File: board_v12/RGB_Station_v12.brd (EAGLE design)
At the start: 86.4 x 17.8 mm, 44 parts, among them IC1 MCP1702T-3302E/MB, J1 M20, J2 M20, J3 USB_MICRO, SW1 KMR2_SWITCH, SW2 KMR2_SWITCH, U1 PIC32MX270F256D_44VTLA_44, U2 74LVC2T45, U3 MCP121T-315E/TT, U4 DSC6111CI1A-008.0000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

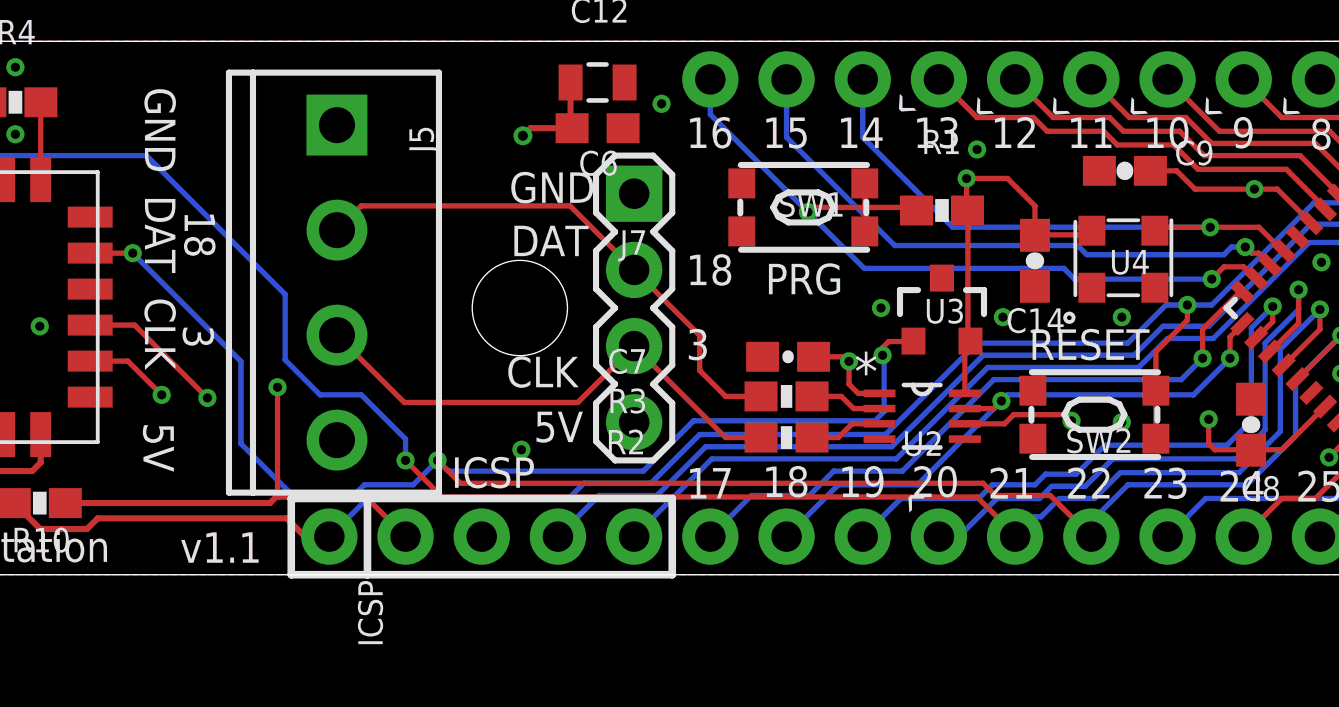
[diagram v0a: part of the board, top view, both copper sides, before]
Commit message: Created v1.2 : fixed schematic problem with switches being always grounded.
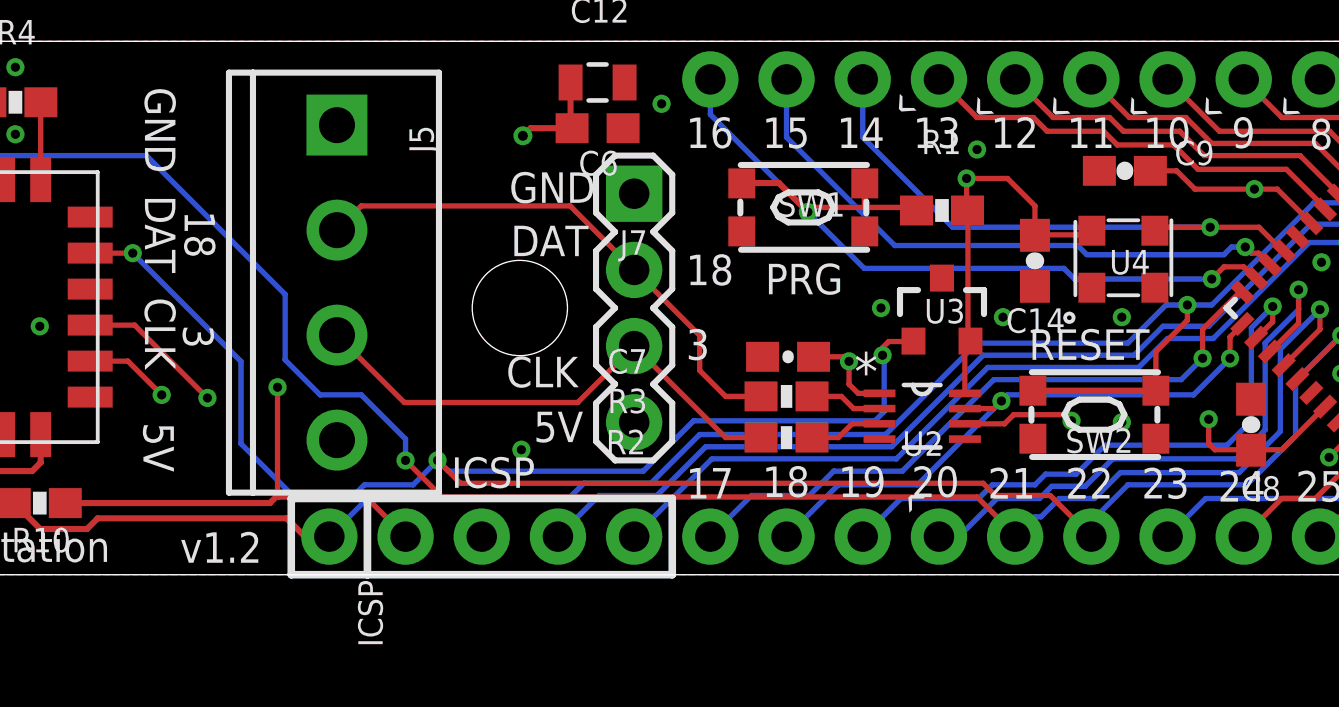
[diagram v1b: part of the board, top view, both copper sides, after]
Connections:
- net !MCLR!: now also SW2.P1; no longer SW2.P3
- net GND: now also SW1.P3, SW2.P3; no longer SW1.P1, SW2.P1
- net RA8: now also SW1.P1; no longer SW1.P3
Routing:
- net !MCLR!: track 90.3 -> 92.8 mm
- net RA8: track 27.4 -> 29.1 mm
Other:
- board text added: "v1.2"
- board text removed: "v1.1"

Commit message: Updates to v1.2 : Made two screw terminals DNPs, and changed C2 from .1uf to 1uF to help with preventing resetting of PIC32 when RN does firmware update.
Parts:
- C2: value .1uF -> 1uF
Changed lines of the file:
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@@
 <?xml version="1.0" encoding="utf-8"?>
 <!DOCTYPE eagle SYSTEM "eagle.dtd">
-<eagle version="7.7.0">
+<eagle version="8.6.2">
 <drawing>
 <settings>
-<setting alwaysvectorfont="yes"/>
+<setting alwaysvectorfont="no"/>
+<setting keepoldvectorfont="yes"/>
 <setting verticaltext="up"/>
 </settings>
@@
 <param name="dpMaxLengthDifference" value="10mm"/>
 <param name="dpGapFactor" value="2.5"/>
-<param name="checkGrid" value="0"/>
 <param name="checkAngle" value="1"/>
 <param name="checkFont" value="1"/>
 <param name="checkRestrict" value="0"/>
+<param name="checkStop" value="0"/>
+<param name="checkValues" value="0"/>
 <param name="useDiameter" value="13"/>
 <param name="maxErrors" value="50"/>
@@
 <element name="U$4" library="SchmalzHausPublic" package="CHIPKIT_2MM" value="CHIPKIT2MM" x="84.99" y="0.6452" rot="MR0"/>
 <element name="J5" library="SparkFun-Connectors" package="SCREWTERMINAL-3.5MM-4@1" value="" x="15.494" y="14.986" smashed="yes" rot="R270">
+<attribute name="NAME" x="17.907" y="14.986" size="0.8128" layer="25" font="vector" ratio="10" rot="R270"/>
+<attribute name="PROD_ID" value="2xCONN-08399" x="-22.606" y="61.976" size="1.778" layer="27" rot="R270" display="off"/>
 <attribute name="SF_ID" value="2xPRT-08084" x="-22.606" y="61.976" size="1.778" layer="27" rot="R270" display="off"/>
-<attribute name="PROD_ID" value="2xCONN-08399" x="-22.606" y="61.976" size="1.778" layer="27" rot="R270" display="off"/>
-<attribute name="NAME" x="17.907" y="14.986" size="0.8128" layer="25" font="vector" ratio="10" rot="R270"/>
 <attribute name="VALUE" x="13.208" y="14.986" size="0.6096" layer="27" font="vector" ratio="20" rot="R270"/>
 </element>
@@
 </element>
 <element name="J7" library="SparkFun-Connectors" package="1X04" value="" x="25.4" y="12.7" smashed="yes" rot="R270">
+<attribute name="NAME" x="24.9174" y="10.668" size="0.8128" layer="25" font="vector" ratio="10"/>
 <attribute name="PROD_ID" value="CONN-09696" x="72.39" y="95.25" size="1.778" layer="27" rot="R270" display="off"/>
-<attribute name="NAME" x="24.9174" y="10.668" size="0.8128" layer="25" font="vector" ratio="10"/>
 <attribute name="VALUE" x="22.225" y="13.97" size="1.27" layer="27" rot="R270"/>
 </element>
@@
 </element>
 <element name="J3" library="SparkFun-Connectors" package="USB-B-MICRO-SMD" value="USB_MICRO" x="84.328" y="5.4356" smashed="yes" rot="R180">
+<attribute name="NAME" x="85.598" y="0.7366" size="0.8128" layer="25" font="vector" ratio="10" rot="R180"/>
 <attribute name="PROD_ID" value="CONN-11752" x="84.328" y="5.4356" size="1.778" layer="27" rot="R180" display="off"/>
-<attribute name="NAME" x="85.598" y="0.7366" size="0.8128" layer="25" font="vector" ratio="10" rot="R180"/>
 <attribute name="VALUE" x="85.598" y="10.1346" size="0.8128" layer="27" font="vector" ratio="10" rot="R180" align="top-left"/>
 </element>
 <element name="J6" library="SparkFun-Connectors" package="SCREWTERMINAL-3.5MM-2" value="" x="81.3308" y="15.6972" smashed="yes" rot="R270">
 <attribute name="NAME" x="84.7598" y="16.9672" size="0.8128" layer="25" font="vector" ratio="10" rot="R270"/>
+<attribute name="PROD_ID" value="CONN-08399" x="81.3308" y="15.6972" size="1.778" layer="27" rot="R270" display="off"/>
 <attribute name="VALUE" x="77.2668" y="16.9672" size="0.6096" layer="27" font="vector" ratio="20" rot="R270"/>
-<attribute name="PROD_ID" value="CONN-08399" x="81.3308" y="15.6972" size="1.778" layer="27" rot="R270" display="off"/>
 </element>
 <element name="U3" library="MCP1x2_ResetController" package="SOT23-3" value="MCP121T-315E/TT" x="35.6616" y="8.7884" smashed="yes">
@@
 <attribute name="VALUE" x="0.4064" y="16.5481" size="0.8128" layer="27" font="vector" ratio="10"/>
 </element>
-<element name="C2" library="SparkFun-Capacitors" package="0603-CAP" value=".1uF" x="2.3876" y="2.3876" smashed="yes">
+<element name="C2" library="SparkFun-Capacitors" package="0603-CAP" value="1uF" x="2.3876" y="2.3876" smashed="yes">
 <attribute name="NAME" x="1.7018" y="0.762" size="0.8128" layer="25" font="vector" ratio="10"/>
 <attribute name="VALUE" x="1.2192" y="-0.5334" size="0.8128" layer="27" font="vector" ratio="10"/>

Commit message: Updated v1.2 board for PCB:NG production - changed DRC rules to minimize violations. Updated .1uF cap and red LED with alternate parts. Updated USB footprint to be exactly correct for Wurth USB connector from BOM
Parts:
- IC1: device linear:SOT89 -> RGB_Station_v12:LINEAR_SOT89
- J3: device SparkFun-Connectors:USB-B-MICRO-SMD -> RGB_Station_v12:SPARKFUN-CONNECTORS_USB-B-MICRO-SMD
- moved J3 0.46 mm to (84.8, 5.44)
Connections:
- removed net N$8: C2.1, U6.5
- new net N$7: C2.1, U6.9
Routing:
- net N$7: track 0.00 -> 15.8 mm, vias 0 -> 2
- net N$8: track 5.58 -> 0.00 mm
- net RC7: track 6.06 -> 5.31 mm
- net USBID/RB5: track 53.7 -> 54.2 mm
- net D-/RB11: track 33.6 -> 34.1 mm
- net D+/RB10: track 36.7 -> 37.2 mm
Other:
- board size 86.4 x 17.8 mm -> 86.4 x 18.2 mm

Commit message: Updated note on schematic about using open-drain reset controller, not push-pull.
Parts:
- U3: value MCP121T-315E/TT -> MCP131T-315E/TT
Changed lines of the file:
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@@
 <attribute name="VALUE" x="77.2668" y="16.9672" size="0.6096" layer="27" font="vector" ratio="20" rot="R270"/>
 </element>
-<element name="U3" library="MCP1x2_ResetController" package="SOT23-3" value="MCP121T-315E/TT" x="35.6616" y="8.7884" smashed="yes">
+<element name="U3" library="MCP1x2_ResetController" package="SOT23-3" value="MCP131T-315E/TT" x="35.6616" y="8.7884" smashed="yes">
 <attribute name="NAME" x="35.068" y="8.3792" size="0.8128" layer="25" font="vector" ratio="10"/>
 <attribute name="VALUE" x="23.5364" y="8.8604" size="0.8128" layer="27" font="vector" ratio="10"/>

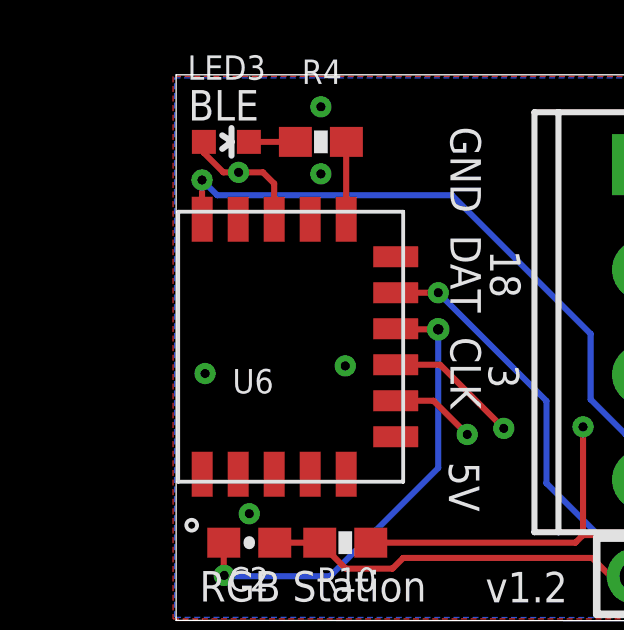
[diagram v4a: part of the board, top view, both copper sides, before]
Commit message: Finished centroid file for PCB:NG automation. Updated some library footprints.
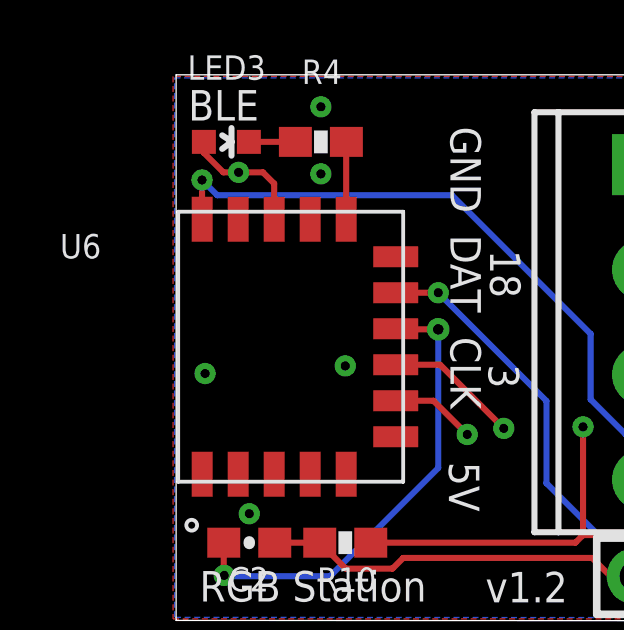
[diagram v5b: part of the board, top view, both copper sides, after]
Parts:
- IC1: device RGB_Station_v12:LINEAR_SOT89 -> RGB_Station_v12_VREG:RGB_STATION_V12_LINEAR_SOT89
- J3: device RGB_Station_v12:SPARKFUN-CONNECTORS_USB-B-MICRO-SMD -> RGB_Station_v12_USB_CONN:SPARKFUN-CONNECTORS_USB-B-MICRO-SMD
- moved U6 7.30 mm to (1.77, 8.92)

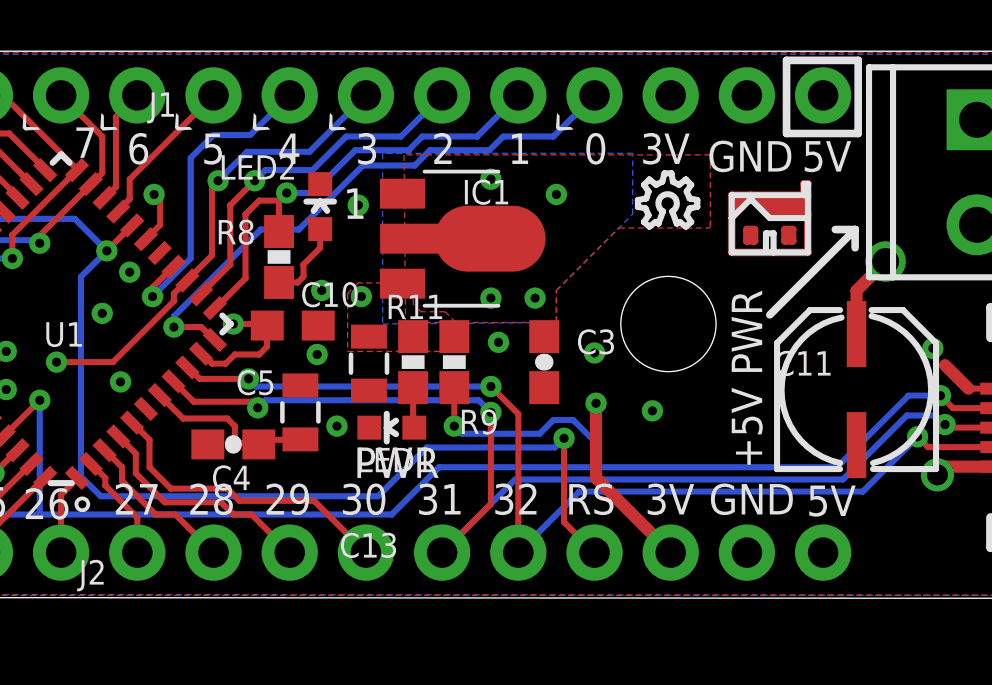
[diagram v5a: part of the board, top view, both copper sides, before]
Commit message: Got all PCB:NG DFM errors to go away - * Added large stop mask rectangles custom versions of USB, level shifter and PIC32 parts to fix stop mask too close errors * Fixed CAM file to include pads layer when generating inner layer gerbers to fix annular ring errors
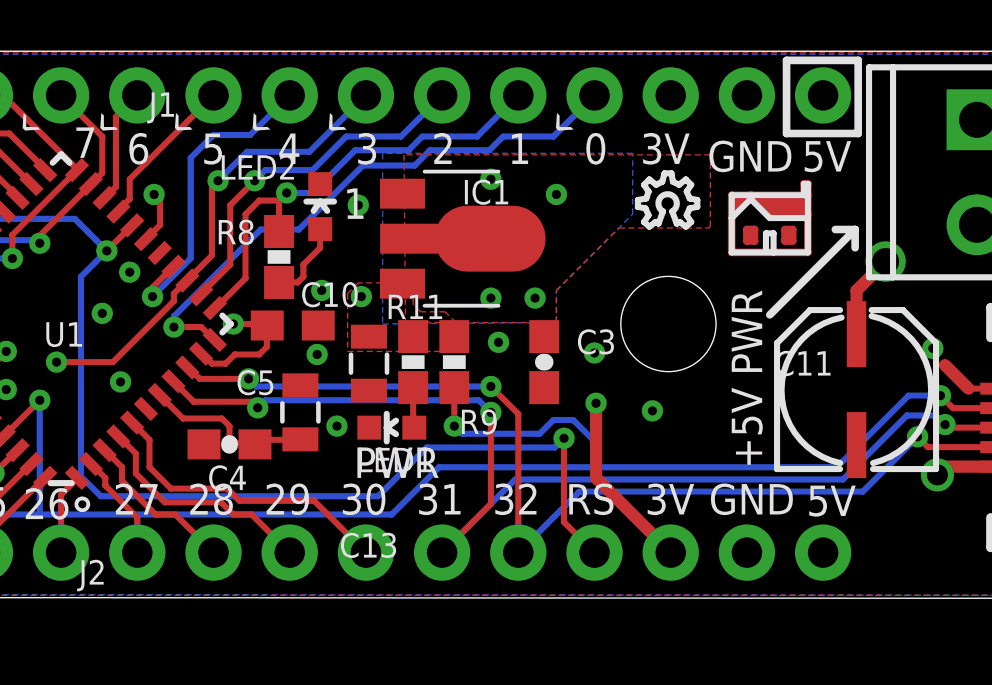
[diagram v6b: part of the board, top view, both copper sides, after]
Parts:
- moved C4 0.13 mm to (56.4, 4.88)
